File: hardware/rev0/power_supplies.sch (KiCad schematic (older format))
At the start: 40 parts, among them IC1 ECP5-BGA256, U2 MIC5504-1.8YM5, U3 MIC5219-3.3YM5, U4 TCR2EF11, U5 MIC5504-2.5YM5

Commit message: hardware: add part numbers
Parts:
- C1, C2, C20, C21, C3, C4, C6: Description (none) -> CAP CER 2.2UF 10V X5R 0603; Manufacturer_Name (none) -> Kemet; Manufacturer_Part_Number (none) -> C0603C225K8PACTU
- C10, C11, C12, C13, C14, C15, C16, C17, C18, C23, C24, C25, C26, C7, C8, C9: Manufacturer_Part_Number (none) -> GENERIC-CAP-0402-0.1uF
- C19, C22, C28, C29, C30, C5: Manufacturer_Part_Number (none) -> GENERIC-CAP-0603-1uF
- C52: Description (none) -> CAP CER 470PF 50V C0G/NP0 0402; Manufacturer_Name (none) -> Kemet; Manufacturer_Part_Number (none) -> C0402C471J5GACTU
- U2: Description (none) -> IC REG LINEAR 1.8V 300MA SOT23-5; Manufacturer_Name (none) -> Microchip; Manufacturer_Part_Number (none) -> MIC5504-1.8YM5-TR
- U3: Description (none) -> IC REG LINEAR 3.3V 500MA SOT23-5; Manufacturer_Name (none) -> Microchip; Manufacturer_Part_Number (none) -> MIC5219-3.3YM5-TR
- U4: Description (none) -> IC REG LINEAR 1.15V 200MA ESV; Manufacturer_Name (none) -> Toshiba; Manufacturer_Part_Number (none) -> TCR2EE115,LM(CT
- U5: Description (none) -> IC REG LINEAR 2.5V 300MA SOT23-5; Manufacturer_Name (none) -> Microchip; Manufacturer_Part_Number (none) -> MIC5504-2.5YM5-TR
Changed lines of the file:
@@
 EESchema Schematic File Version 4
-LIBS:luna_rev0-cache
 EELAYER 30 0
 EELAYER END
@@
 F 2 "Package_TO_SOT_SMD:SOT-23-5" H 2250 5950 50  0001 C CNN
 F 3 "http://ww1.microchip.com/downloads/en/DeviceDoc/MIC550X.pdf" H 2000 6600 50  0001 C CNN
+F 4 "IC REG LINEAR 1.8V 300MA SOT23-5" H 2250 6350 50  0001 C CNN "Description"
+F 5 "Microchip" H 2250 6350 50  0001 C CNN "Manufacturer_Name"
+F 6 "MIC5504-1.8YM5-TR" H 2250 6350 50  0001 C CNN "Manufacturer_Part_Number"
 	1    2250 6350
 	1    0    0    -1
@@
 F 2 "Capacitor_SMD:C_0603_1608Metric" H 1388 5900 50  0001 C CNN
 F 3 "~" H 1350 6050 50  0001 C CNN
+F 4 "GENERIC-CAP-0603-1uF" H 1350 6050 50  0001 C CNN "Manufacturer_Part_Number"
 	1    1350 6050
 	0    1    1    0
@@
 F 2 "Capacitor_SMD:C_0603_1608Metric" H 2838 6250 50  0001 C CNN
 F 3 "~" H 2800 6400 50  0001 C CNN
+F 4 "GENERIC-CAP-0603-1uF" H 2800 6400 50  0001 C CNN "Manufacturer_Part_Number"
 	1    2800 6400
 	1    0    0    -1
@@
 F 2 "Capacitor_SMD:C_0603_1608Metric" H 4488 5900 50  0001 C CNN
 F 3 "~" H 4450 6050 50  0001 C CNN
+F 4 "GENERIC-CAP-0603-1uF" H 4450 6050 50  0001 C CNN "Manufacturer_Part_Number"
 	1    4450 6050
 	0    1    1    0
@@
 F 2 "Capacitor_SMD:C_0603_1608Metric" H 5938 6250 50  0001 C CNN
 F 3 "~" H 5900 6400 50  0001 C CNN
+F 4 "GENERIC-CAP-0603-1uF" H 5900 6400 50  0001 C CNN "Manufacturer_Part_Number"
 	1    5900 6400
 	1    0    0    -1
@@
 F 2 "Package_TO_SOT_SMD:SOT-23-5" H 5350 5950 50  0001 C CNN
 F 3 "http://ww1.microchip.com/downloads/en/DeviceDoc/MIC550X.pdf" H 5100 6600 50  0001 C CNN
+F 4 "IC REG LINEAR 2.5V 300MA SOT23-5" H 5350 6350 50  0001 C CNN "Description"
+F 5 "Microchip" H 5350 6350 50  0001 C CNN "Manufacturer_Name"
+F 6 "MIC5504-2.5YM5-TR" H 5350 6350 50  0001 C CNN "Manufacturer_Part_Number"
 	1    5350 6350
 	1    0    0    -1
@@
 F 2 "Capacitor_SMD:C_0603_1608Metric" H 1488 3750 50  0001 C CNN
 F 3 "~" H 1450 3900 50  0001 C CNN
+F 4 "CAP CER 2.2UF 10V X5R 0603" H 1450 3900 50  0001 C CNN "Description"
+F 5 "Kemet" H 1450 3900 50  0001 C CNN "Manufacturer_Name"
+F 6 "C0603C225K8PACTU" H 1450 3900 50  0001 C CNN "Manufacturer_Part_Number"
 	1    1450 3900
 	0    1    1    0
@@
 F 2 "Capacitor_SMD:C_0603_1608Metric" H 2988 4100 50  0001 C CNN
 F 3 "~" H 2950 4250 50  0001 C CNN
+F 4 "CAP CER 2.2UF 10V X5R 0603" H 2950 4250 50  0001 C CNN "Description"
+F 5 "Kemet" H 2950 4250 50  0001 C CNN "Manufacturer_Name"
+F 6 "C0603C225K8PACTU" H 2950 4250 50  0001 C CNN "Manufacturer_Part_Number"
 	1    2950 4250
 	1    0    0    -1
@@
 F 2 "Capacitor_SMD:C_0603_1608Metric" H 5938 4050 50  0001 C CNN
 F 3 "~" H 5900 4200 50  0001 C CNN
+F 4 "GENERIC-CAP-0603-1uF" H 5900 4200 50  0001 C CNN "Manufacturer_Part_Number"
 	1    5900 4200
 	1    0    0    -1
@@
 F 2 "Package_TO_SOT_SMD:SOT-553" H 5350 3750 50  0001 C CNN
 F 3 "https://toshiba.semicon-storage.com/info/docget.jsp?did=13794&prodName=TCR2EF45" H 5100 4400 50  0001 C CNN
+F 4 "IC REG LINEAR 1.15V 200MA ESV" H 5350 4150 50  0001 C CNN "Description"
+F 5 "Toshiba" H 5350 4150 50  0001 C CNN "Manufacturer_Name"
+F 6 "TCR2EE115,LM(CT" H 5350 4150 50  0001 C CNN "Manufacturer_Part_Number"
 	1    5350 4150
 	1    0    0    -1
@@
 F 2 "Capacitor_SMD:C_0402_1005Metric" H 1738 850 50  0001 C CNN
 F 3 "~" H 1700 1000 50  0001 C CNN
+F 4 "GENERIC-CAP-0402-0.1uF" H 1700 1000 50  0001 C CNN "Manufacturer_Part_Number"
 	1    1700 1000
 	1    0    0    -1
@@
 F 2 "Capacitor_SMD:C_0402_1005Metric" H 1938 850 50  0001 C CNN
 F 3 "~" H 1900 1000 50  0001 C CNN
+F 4 "GENERIC-CAP-0402-0.1uF" H 1900 1000 50  0001 C CNN "Manufacturer_Part_Number"
 	1    1900 1000
 	1    0    0    -1
@@
 F 2 "Capacitor_SMD:C_0402_1005Metric" H 2138 850 50  0001 C CNN
 F 3 "~" H 2100 1000 50  0001 C CNN
+F 4 "GENERIC-CAP-0402-0.1uF" H 2100 1000 50  0001 C CNN "Manufacturer_Part_Number"
 	1    2100 1000
 	1    0    0    -1
@@
 F 2 "Capacitor_SMD:C_0402_1005Metric" H 2338 850 50  0001 C CNN
 F 3 "~" H 2300 1000 50  0001 C CNN
+F 4 "GENERIC-CAP-0402-0.1uF" H 2300 1000 50  0001 C CNN "Manufacturer_Part_Number"
 	1    2300 1000
 	1    0    0    -1
@@
 F 2 "Capacitor_SMD:C_0402_1005Metric" H 2538 850 50  0001 C CNN
 F 3 "~" H 2500 1000 50  0001 C CNN
+F 4 "GENERIC-CAP-0402-0.1uF" H 2500 1000 50  0001 C CNN "Manufacturer_Part_Number"
 	1    2500 1000
 	1    0    0    -1
@@
 F 2 "Capacitor_SMD:C_0402_1005Metric" H 2738 850 50  0001 C CNN
 F 3 "~" H 2700 1000 50  0001 C CNN
+F 4 "GENERIC-CAP-0402-0.1uF" H 2700 1000 50  0001 C CNN "Manufacturer_Part_Number"
 	1    2700 1000
 	1    0    0    -1
@@
 F 2 "Capacitor_SMD:C_0603_1608Metric" H 1088 850 50  0001 C CNN
 F 3 "~" H 1050 1000 50  0001 C CNN
+F 4 "CAP CER 2.2UF 10V X5R 0603" H 1050 1000 50  0001 C CNN "Description"
+F 5 "Kemet" H 1050 1000 50  0001 C CNN "Manufacturer_Name"
+F 6 "C0603C225K8PACTU" H 1050 1000 50  0001 C CNN "Manufacturer_Part_Number"
 	1    1050 1000
 	1    0    0    -1
@@
 F 2 "Capacitor_SMD:C_0603_1608Metric" H 1288 850 50  0001 C CNN
 F 3 "~" H 1250 1000 50  0001 C CNN
+F 4 "CAP CER 2.2UF 10V X5R 0603" H 1250 1000 50  0001 C CNN "Description"
+F 5 "Kemet" H 1250 1000 50  0001 C CNN "Manufacturer_Name"
+F 6 "C0603C225K8PACTU" H 1250 1000 50  0001 C CNN "Manufacturer_Part_Number"
 	1    1250 1000
 	1    0    0    -1
@@
 F 2 "Capacitor_SMD:C_0603_1608Metric" H 1288 1850 50  0001 C CNN
 F 3 "~" H 1250 2000 50  0001 C CNN
+F 4 "CAP CER 2.2UF 10V X5R 0603" H 1250 2000 50  0001 C CNN "Description"
+F 5 "Kemet" H 1250 2000 50  0001 C CNN "Manufacturer_Name"
+F 6 "C0603C225K8PACTU" H 1250 2000 50  0001 C CNN "Manufacturer_Part_Number"
 	1    1250 2000
 	1    0    0    -1
@@
 F 2 "Capacitor_SMD:C_0603_1608Metric" H 1088 1850 50  0001 C CNN
 F 3 "~" H 1050 2000 50  0001 C CNN
+F 4 "CAP CER 2.2UF 10V X5R 0603" H 1050 2000 50  0001 C CNN "Description"
+F 5 "Kemet" H 1050 2000 50  0001 C CNN "Manufacturer_Name"
+F 6 "C0603C225K8PACTU" H 1050 2000 50  0001 C CNN "Manufacturer_Part_Number"
 	1    1050 2000
 	1    0    0    -1
@@
 F 2 "Capacitor_SMD:C_0402_1005Metric" H 2738 1850 50  0001 C CNN
 F 3 "~" H 2700 2000 50  0001 C CNN
+F 4 "GENERIC-CAP-0402-0.1uF" H 2700 2000 50  0001 C CNN "Manufacturer_Part_Number"
 	1    2700 2000
 	1    0    0    -1
@@
 F 2 "Capacitor_SMD:C_0402_1005Metric" H 2538 1850 50  0001 C CNN
 F 3 "~" H 2500 2000 50  0001 C CNN
+F 4 "GENERIC-CAP-0402-0.1uF" H 2500 2000 50  0001 C CNN "Manufacturer_Part_Number"
 	1    2500 2000
 	1    0    0    -1
@@
 F 2 "Capacitor_SMD:C_0402_1005Metric" H 2338 1850 50  0001 C CNN
 F 3 "~" H 2300 2000 50  0001 C CNN
+F 4 "GENERIC-CAP-0402-0.1uF" H 2300 2000 50  0001 C CNN "Manufacturer_Part_Number"
 	1    2300 2000
 	1    0    0    -1
@@
 F 2 "Capacitor_SMD:C_0402_1005Metric" H 2138 1850 50  0001 C CNN
 F 3 "~" H 2100 2000 50  0001 C CNN
+F 4 "GENERIC-CAP-0402-0.1uF" H 2100 2000 50  0001 C CNN "Manufacturer_Part_Number"
 	1    2100 2000
 	1    0    0    -1
@@
 F 2 "Capacitor_SMD:C_0402_1005Metric" H 1938 1850 50  0001 C CNN
 F 3 "~" H 1900 2000 50  0001 C CNN
+F 4 "GENERIC-CAP-0402-0.1uF" H 1900 2000 50  0001 C CNN "Manufacturer_Part_Number"
 	1    1900 2000
 	1    0    0    -1
@@
 F 2 "Capacitor_SMD:C_0402_1005Metric" H 1738 1850 50  0001 C CNN
 F 3 "~" H 1700 2000 50  0001 C CNN
+F 4 "GENERIC-CAP-0402-0.1uF" H 1700 2000 50  0001 C CNN "Manufacturer_Part_Number"
 	1    1700 2000
 	1    0    0    -1
@@
 F 2 "Capacitor_SMD:C_0603_1608Metric" H 3888 850 50  0001 C CNN
 F 3 "~" H 3850 1000 50  0001 C CNN
+F 4 "GENERIC-CAP-0603-1uF" H 3850 1000 50  0001 C CNN "Manufacturer_Part_Number"
 	1    3850 1000
 	1    0    0    -1
@@
 F 2 "Capacitor_SMD:C_0402_1005Metric" H 4238 850 50  0001 C CNN
 F 3 "~" H 4200 1000 50  0001 C CNN
+F 4 "GENERIC-CAP-0402-0.1uF" H 4200 1000 50  0001 C CNN "Manufacturer_Part_Number"
 	1    4200 1000
 	1    0    0    -1
@@
 F 2 "Capacitor_SMD:C_0402_1005Metric" H 4438 850 50  0001 C CNN
 F 3 "~" H 4400 1000 50  0001 C CNN
+F 4 "GENERIC-CAP-0402-0.1uF" H 4400 1000 50  0001 C CNN "Manufacturer_Part_Number"
 	1    4400 1000
 	1    0    0    -1
@@
 F 2 "Capacitor_SMD:C_0603_1608Metric" H 3838 1850 50  0001 C CNN
 F 3 "~" H 3800 2000 50  0001 C CNN
+F 4 "CAP CER 2.2UF 10V X5R 0603" H 3800 2000 50  0001 C CNN "Description"
+F 5 "Kemet" H 3800 2000 50  0001 C CNN "Manufacturer_Name"
+F 6 "C0603C225K8PACTU" H 3800 2000 50  0001 C CNN "Manufacturer_Part_Number"
 	1    3800 2000
 	1    0    0    -1
@@
 F 2 "Capacitor_SMD:C_0402_1005Metric" H 4188 1850 50  0001 C CNN
 F 3 "~" H 4150 2000 50  0001 C CNN
+F 4 "GENERIC-CAP-0402-0.1uF" H 4150 2000 50  0001 C CNN "Manufacturer_Part_Number"
 	1    4150 2000
 	1    0    0    -1
@@
 F 2 "Capacitor_SMD:C_0402_1005Metric" H 4388 1850 50  0001 C CNN
 F 3 "~" H 4350 2000 50  0001 C CNN
+F 4 "GENERIC-CAP-0402-0.1uF" H 4350 2000 50  0001 C CNN "Manufacturer_Part_Number"
 	1    4350 2000
 	1    0    0    -1
@@
 F 2 "Capacitor_SMD:C_0402_1005Metric" H 2688 4300 50  0001 C CNN
 F 3 "~" H 2650 4450 50  0001 C CNN
+F 4 "CAP CER 470PF 50V C0G/NP0 0402" H 2650 4450 50  0001 C CNN "Description"
+F 5 "Kemet" H 2650 4450 50  0001 C CNN "Manufacturer_Name"
+F 6 "C0402C471J5GACTU" H 2650 4450 50  0001 C CNN "Manufacturer_Part_Number"
 	1    2650 4450
 	1    0    0    -1
@@
 F 2 "Package_TO_SOT_SMD:SOT-23-5" H 2350 4525 50  0001 C CNN
 F 3 "http://ww1.microchip.com/downloads/en/DeviceDoc/MIC5219-500mA-Peak-Output-LDO-Regulator-DS20006021A.pdf" H 2350 4200 50  0001 C CNN
+F 4 "IC REG LINEAR 3.3V 500MA SOT23-5" H 2350 4200 50  0001 C CNN "Description"
+F 5 "Microchip" H 2350 4200 50  0001 C CNN "Manufacturer_Name"
+F 6 "MIC5219-3.3YM5-TR" H 2350 4200 50  0001 C CNN "Manufacturer_Part_Number"
 	1    2350 4200
 	1    0    0    -1

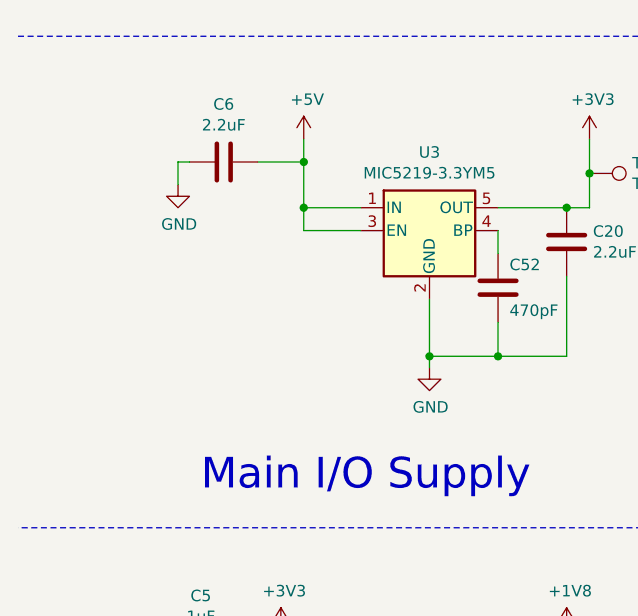
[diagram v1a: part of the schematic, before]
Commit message: hardware: update capacitors in schematic
Add parts that were in layout but were missing from schematic.
Update schematic to better represent r0.2 as manufactured.
fix #10
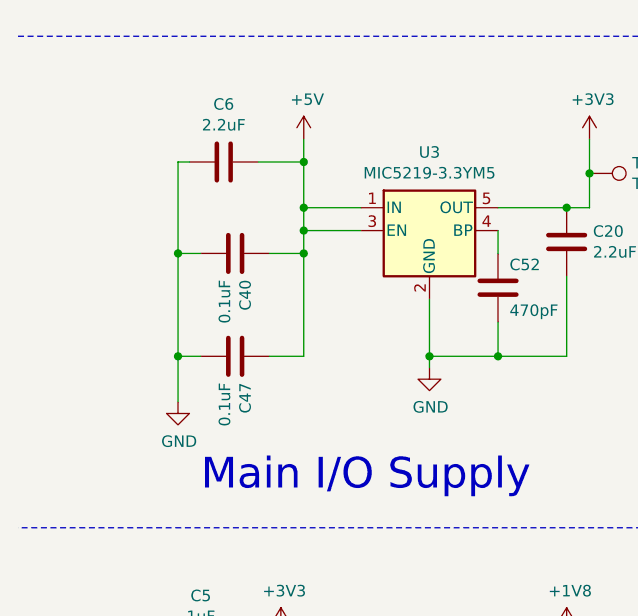
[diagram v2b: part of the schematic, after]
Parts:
- added C40, C47: 0.1uF, Capacitor_SMD:C_0402_1005Metric, symbol Device:C
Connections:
- wire segments 156 -> 164

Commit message: hardware: Change U4 to match part number
Update value and symbol name from TCR2EF11 to TCR2EE11.
fix #12
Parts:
- U4: value TCR2EF11 -> TCR2EE11; symbol support_hardware:TCR2EF11 -> support_hardware:TCR2EE11
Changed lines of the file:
@@
 	550  3350 7000 3350
 $Comp
-L support_hardware:TCR2EF11 U4
+L support_hardware:TCR2EE11 U4
 U 1 1 5DB6F5E4
 P 5350 4150
 F 0 "U4" H 5350 4517 50  0000 C CNN
-F 1 "TCR2EF11" H 5350 4426 50  0000 C CNN
+F 1 "TCR2EE11" H 5350 4426 50  0000 C CNN
 F 2 "Package_TO_SOT_SMD:SOT-553" H 5350 3750 50  0001 C CNN
 F 3 "https://toshiba.semicon-storage.com/info/docget.jsp?did=13794&prodName=TCR2EF45" H 5100 4400 50  0001 C CNN

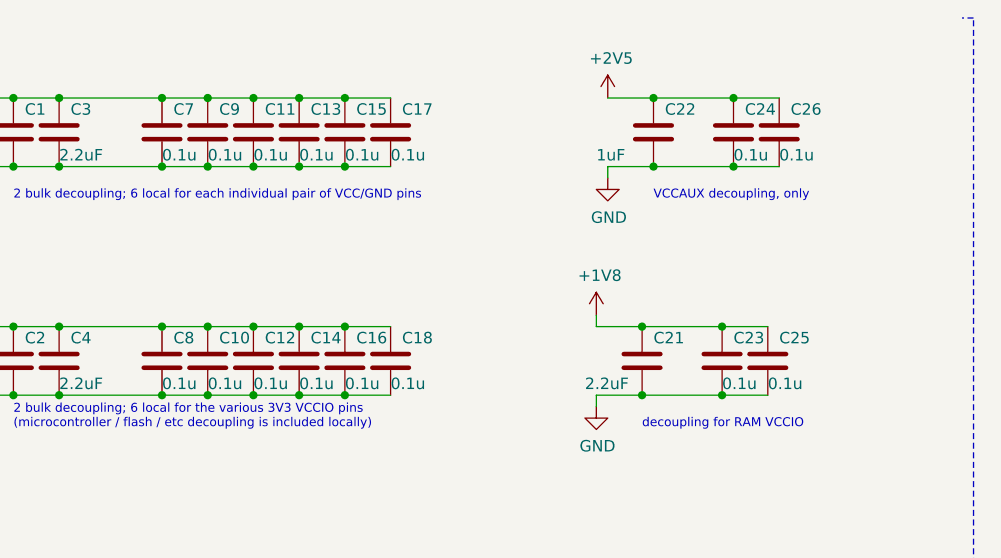
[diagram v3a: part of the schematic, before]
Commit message: hardware: normalize BOM fields
make compatible with kicad-bom-scripts
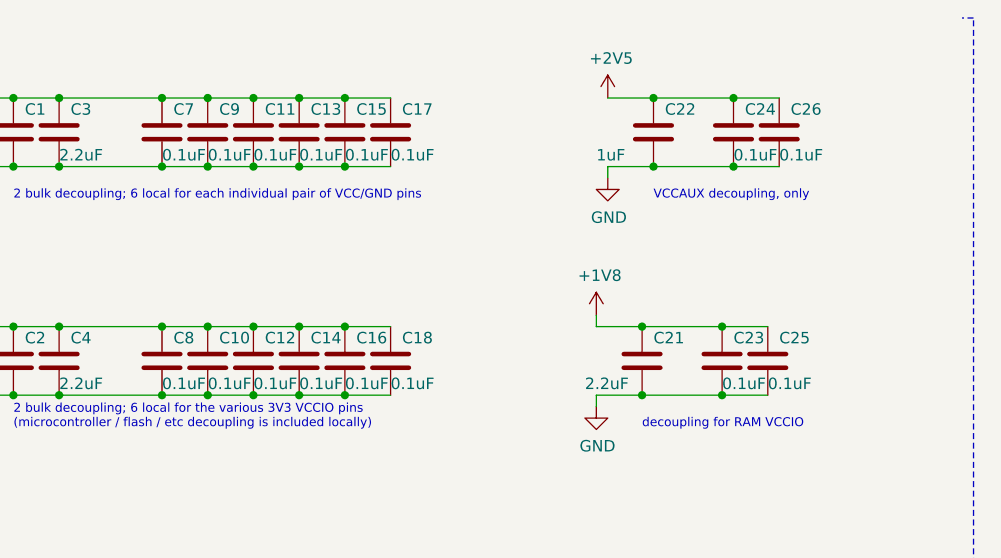
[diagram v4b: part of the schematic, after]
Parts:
- C1, C2, C20, C21, C3, C4, C6: Manufacturer (none) -> Kemet; Manufacturer_Name Kemet -> (none); Manufacturer_Part_Number C0603C225K8PACTU -> (none); Part Number (none) -> C0603C225K8PACTU
- C10, C11, C12, C13, C14, C15, C16, C17, C18, C23, C24, C25, C26, C7, C8, C9: value 0.1u -> 0.1uF; Manufacturer_Part_Number GENERIC-CAP-0402-0.1uF -> (none); Part Number (none) -> GENERIC-CAP-0402-0.1uF
- C19, C22, C28, C29, C30, C5: Manufacturer_Part_Number GENERIC-CAP-0603-1uF -> (none); Part Number (none) -> GENERIC-CAP-0603-1uF
- C27, C40, C47: Part Number (none) -> GENERIC-CAP-0402-0.1uF
- C52: Manufacturer (none) -> Kemet; Manufacturer_Name Kemet -> (none); Manufacturer_Part_Number C0402C471J5GACTU -> (none); Part Number (none) -> C0402C471J5GACTU
- IC1: Height 1.7 -> (none); Manufacturer (none) -> Lattice; Manufacturer_Name Lattice -> (none); Manufacturer_Part_Number LFE5U-12F-6BG256C -> (none); Mouser Part Number 842-LFE5U12F6BG256C -> (none); Mouser Price/Stock https://www.mouser.com/Search/Refine.aspx?Keyword=842-LFE5U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 -> (none); Part Number (none) -> LFE5U-12F-6BG256C
- U2: Manufacturer (none) -> Microchip; Manufacturer_Name Microchip -> (none); Manufacturer_Part_Number MIC5504-1.8YM5-TR -> (none); Part Number (none) -> MIC5504-1.8YM5-TR
- U3: Manufacturer (none) -> Microchip; Manufacturer_Name Microchip -> (none); Manufacturer_Part_Number MIC5219-3.3YM5-TR -> (none); Part Number (none) -> MIC5219-3.3YM5-TR
- U4: Manufacturer (none) -> Toshiba; Manufacturer_Name Toshiba -> (none); Manufacturer_Part_Number TCR2EE115,LM(CT -> (none); Part Number (none) -> TCR2EE115,LM(CT
- U5: Manufacturer (none) -> Microchip; Manufacturer_Name Microchip -> (none); Manufacturer_Part_Number MIC5504-2.5YM5-TR -> (none); Part Number (none) -> MIC5504-2.5YM5-TR
